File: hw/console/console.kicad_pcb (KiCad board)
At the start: 2 copper layers, 156 x 74 mm, 161 parts, among them J1 Batt, J301 USB-C 16P, J401 DM3AT-SF-PEJM5, J501 SPK 8R, J601 FFC-40 0.5mm, J901 UART, Q601 AO3400A, SW1 Движок, SW101 UP, SW102 DOWN, SW103 LEFT, SW104 RIGHT, SW105 SELECT, SW106 START, SW107 A, SW108 B, SW109 C, SW110 D, U1 F133-A, U2 SY8089AAAC, U3 SY8089AAAC, U4 SY8089AAAC, U401 W25Q32JVSSIQ, U5 TP4056, U501 PAM8301, Y1 24 МГц, Y2 32.768 кГц

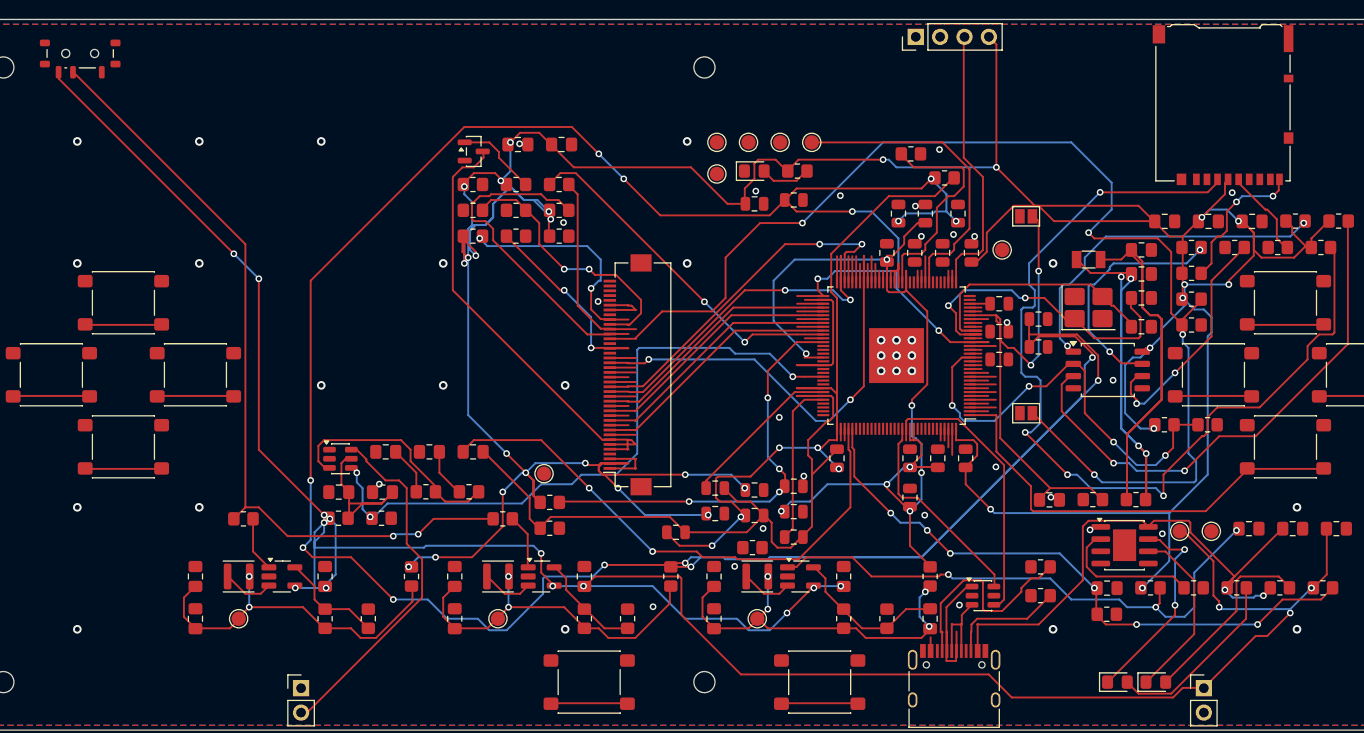
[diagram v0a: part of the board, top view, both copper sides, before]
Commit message: hw: плата на SPI разведена — 196 связей, 56 разрывов
Против параллельной версии: 203/67 при 270 нужных связях стало 196/56 при 252.
Меди 1198 отрезков, заклёпок 216 — их паять руками с двух сторон.

Нарушений DRC одно, проверенное: контур `J601` нарисован в библиотеке
прямоугольником, а на плате полигоном; все 41 площадка совпадает и по имени,
и по месту.

Co-Authored-By: Claude Opus 5 (1M context) <noreply@anthropic.com>
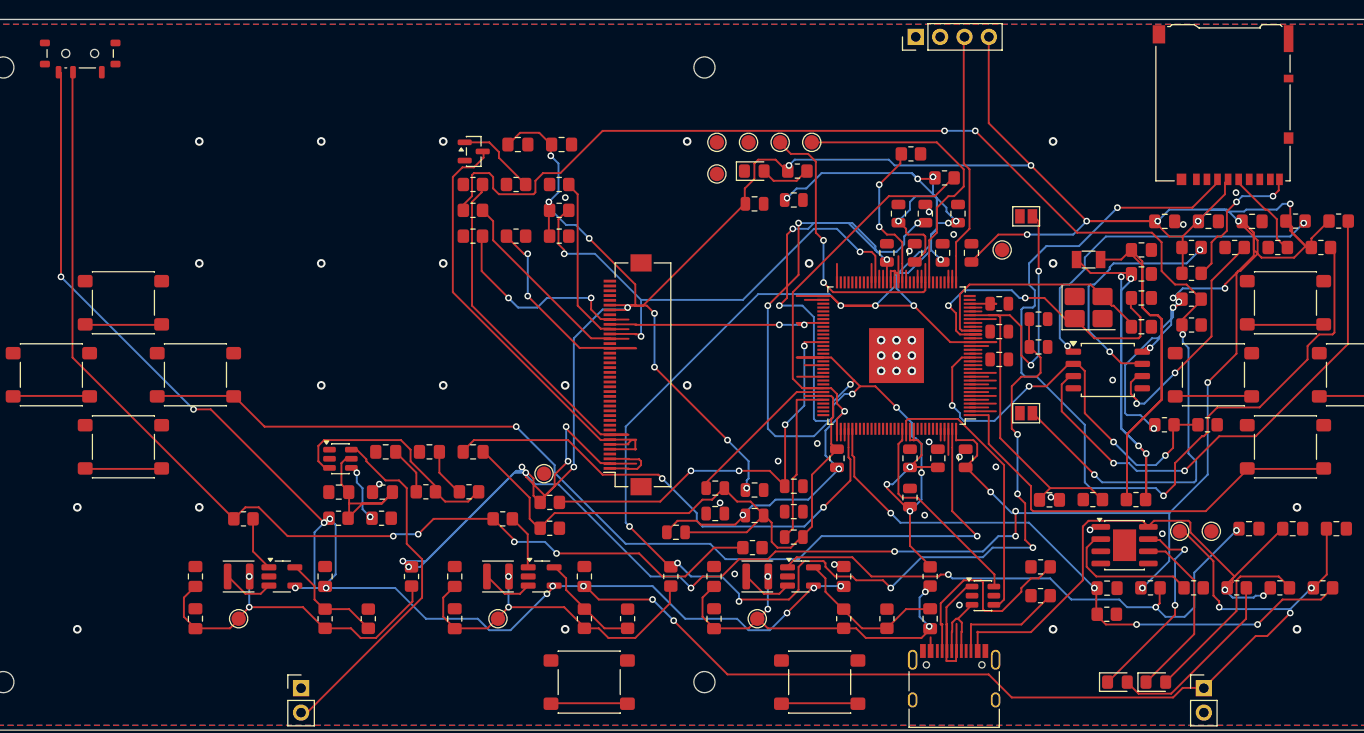
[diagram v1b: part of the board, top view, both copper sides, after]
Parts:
- removed R605: 33, Resistor_SMD:R_0805_2012Metric_Pad1.20x1.40mm_HandSolder
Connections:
- net LCD-WR renamed LCD-SCL
- J601 pad 10: LCD-RS -> LCD-DC
- J601 pad 13: SPI0-MOSI -> LCD-SDA
- J601 pad 17: LCD-DB0 -> GND
- J601 pad 18: LCD-DB1 -> GND
- J601 pad 19: LCD-DB2 -> GND
- J601 pad 20: LCD-DB3 -> GND
- J601 pad 21: LCD-DB4 -> GND
- J601 pad 22: LCD-DB5 -> GND
- J601 pad 23: LCD-DB6 -> GND
- J601 pad 24: LCD-DB7 -> GND
- J601 pad 25: LCD-DB8 -> GND
- J601 pad 26: LCD-DB9 -> GND
- J601 pad 27: LCD-DB11 -> GND
- J601 pad 28: LCD-DB10 -> GND
- J601 pad 29: LCD-DB12 -> GND
- J601 pad 30: LCD-DB13 -> GND
- J601 pad 31: LCD-DB14 -> GND
- J601 pad 32: LCD-DB15 -> GND
- R603 pad 1: LCD0-CLK -> SPI0-CLK
- R604 pad 1: LCD0-DE -> SPI0-MOSI
- R604 pad 2: LCD-RS -> LCD-SDA
- U1 pad 56: LCD-DB0 -> unconnected-(U1-PD1-Pad56)
- U1 pad 57: LCD-DB1 -> unconnected-(U1-PD2-Pad57)
- U1 pad 58: LCD-DB2 -> unconnected-(U1-PD3-Pad58)
- U1 pad 59: LCD-DB3 -> unconnected-(U1-PD4-Pad59)
- U1 pad 60: LCD-DB4 -> unconnected-(U1-PD5-Pad60)
- U1 pad 61: LCD-DB5 -> unconnected-(U1-PD6-Pad61)
- U1 pad 62: LCD-DB6 -> unconnected-(U1-PD7-Pad62)
- U1 pad 63: LCD-DB7 -> unconnected-(U1-PD8-Pad63)
- U1 pad 67: LCD-DB8 -> unconnected-(U1-PD10-Pad67)
- U1 pad 68: LCD-DB9 -> unconnected-(U1-PD11-Pad68)
- U1 pad 69: LCD-DB11 -> unconnected-(U1-PD13-Pad69)
- U1 pad 70: LCD-DB10 -> unconnected-(U1-PD12-Pad70)
- U1 pad 71: LCD-DB12 -> unconnected-(U1-PD14-Pad71)
- U1 pad 72: LCD-DB13 -> LCD-DC
- U1 pad 73: LCD-DB14 -> unconnected-(U1-PD16-Pad73)
- U1 pad 74: LCD-DB15 -> unconnected-(U1-PD17-Pad74)
- U1 pad 75: LCD0-CLK -> unconnected-(U1-PD18-Pad75)
- U1 pad 76: LCD0-DE -> unconnected-(U1-PD19-Pad76)
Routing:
- net +1V8: track 345.3 -> 234.2 mm, vias 16 -> 17
- net KEY-RIGHT: track 10.7 -> 106.1 mm, vias 0 -> 2
- net AMP-SD: track 68.3 -> 9.04 mm, vias 3 -> 2
- net +3V3: track 444.5 -> 492.2 mm, vias 29 -> 36
- net LCD-DB1: track 47.2 -> 0.00 mm, vias 2 -> 0
- net +0V9: track 104.9 -> 149.3 mm, vias 8 -> 13
- net LCD-DB6: track 37.6 -> 0.00 mm, vias 2 -> 0
- net LCD-DB7: track 37.5 -> 0.00 mm, vias 2 -> 0
- net LCD0-CLK: track 36.6 -> 0.00 mm, vias 2 -> 0
- net LCD-LEDA: track 2.75 -> 36.7 mm
- net /PWR_EN: track 82.3 -> 112.9 mm, vias 2 -> 4
- net TDO: track 2.72 -> 31.4 mm, vias 0 -> 2
- net LCD-RS: track 27.9 -> 0.00 mm, vias 2 -> 0
- net LCD-DB15: track 26.6 -> 0.00 mm
- net LCD-DB13: track 26.5 -> 0.00 mm
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
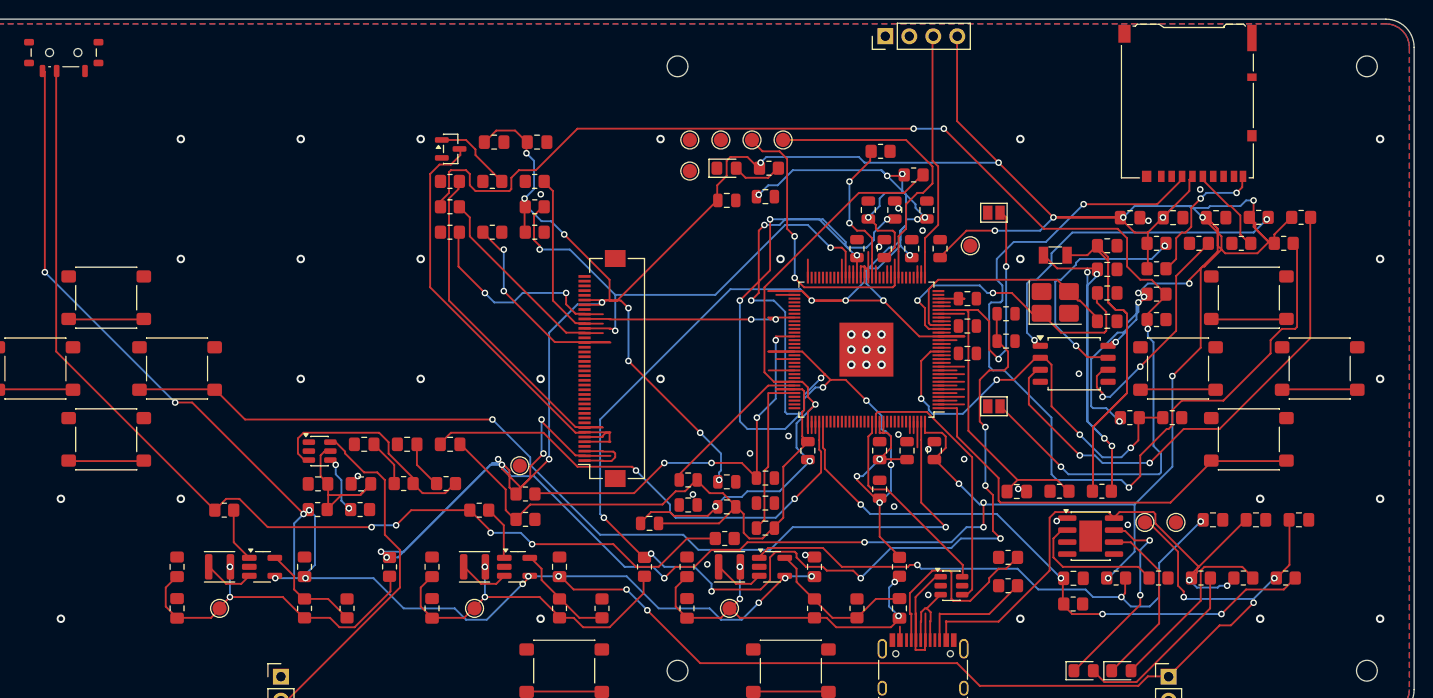
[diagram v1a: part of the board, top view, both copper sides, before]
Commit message: hw: обвязка флешки — к флешке, а не рядами в поле
Увидено заказчиком на снимке платы: `U401` стоит у выводов корпуса, а её девять
резисторов и конденсатор выложены ровным рядом в двух сантиметрах, и каждый
тянет провод обратно. По числам это выглядело просто «связь разведена».

Причина была записана в документе и мной же сегодня стёрта: `pcb03_blocks.py`
кладёт детали внутри зоны ПО РАЗМЕРУ и про связи не знает вовсе. Я заменил эту
запись своим выводом «размещение не узкое место» — вывод строился на шести
опытах, но ни один из них не двигал обвязку к её хозяину.

Теперь `pcb04_fine.py` ставит развязку, подтяжки и страпы относительно самой
`U401`: было 20…25 мм, стало 3.6…8.7.

Co-Authored-By: Claude Opus 5 (1M context) <noreply@anthropic.com>
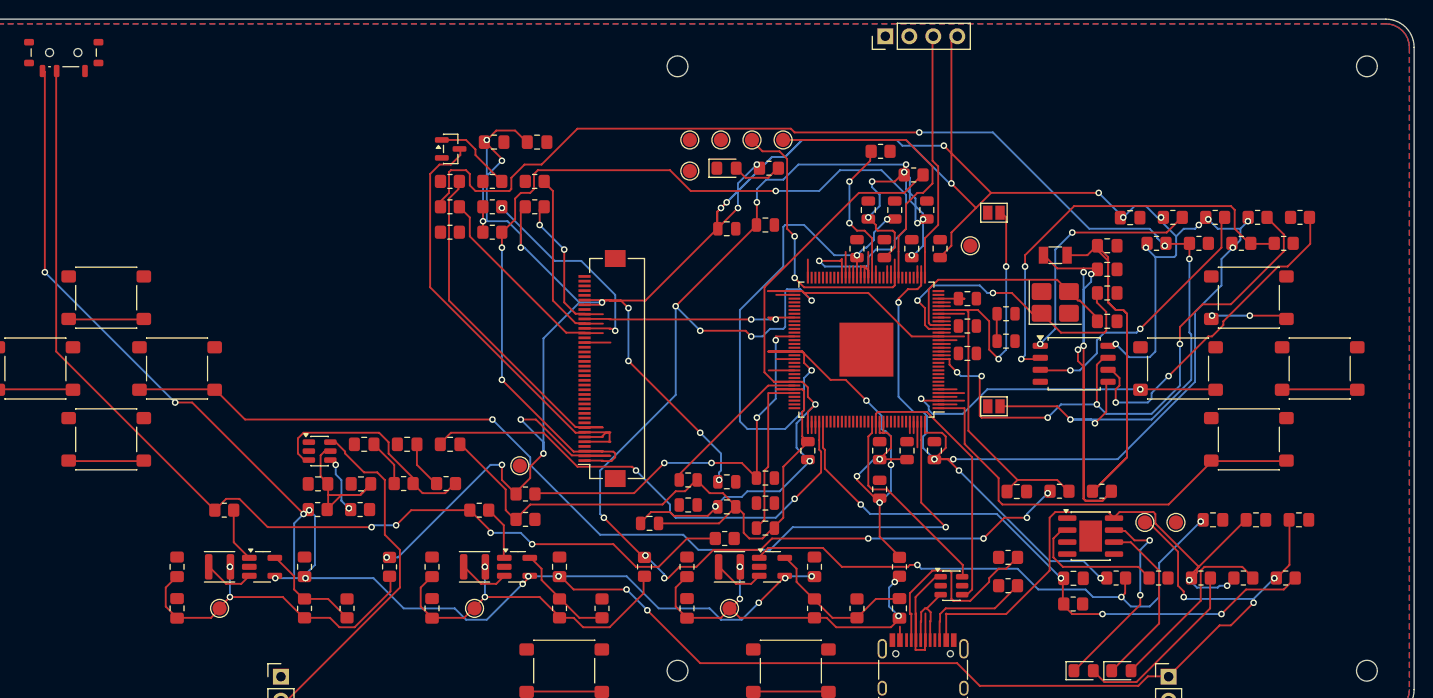
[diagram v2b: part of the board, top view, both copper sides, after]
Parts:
- removed C402: 0.1u, Capacitor_SMD:C_0805_2012Metric_Pad1.18x1.45mm_HandSolder
- removed C403: 10u, Capacitor_SMD:C_0805_2012Metric_Pad1.18x1.45mm_HandSolder
- removed J401: DM3AT-SF-PEJM5, Connector_Card:microSD_HC_Hirose_DM3AT-SF-PEJM5
- removed R405: 33, Resistor_SMD:R_0805_2012Metric_Pad1.20x1.40mm_HandSolder
- removed R406, R407: 10k, Resistor_SMD:R_0805_2012Metric_Pad1.20x1.40mm_HandSolder
- moved R411 21.9 mm to (192.2, 63.7)
- moved R410 21.9 mm to (187.7, 63.7)
- moved R403 11.1 mm to (189.4, 61.0)
- moved R404 11.1 mm to (193.9, 61.0)
- moved R607 9.37 mm to (112.9, 59.9)
- moved R409 9.23 mm to (183.2, 63.7)
- moved R401 9.10 mm to (180.4, 61.0)
- moved R402 9.10 mm to (184.9, 61.0)
- moved R408 5.38 mm to (178.7, 63.7)
- moved R608 4.49 mm to (103.9, 62.6)
- moved R606 4.49 mm to (108.4, 59.9)
- moved R609 4.49 mm to (108.4, 62.6)
- moved C803 3.00 mm to (133.2, 62.2)
- moved C812 3.00 mm to (137.3, 61.8)
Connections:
- U1 pad 10: SDC0-CMD -> unconnected-(U1-PF3-Pad10)
- U1 pad 11: SDC0-D3 -> unconnected-(U1-PF4-Pad11)
- U1 pad 12: SDC0-D2 -> unconnected-(U1-PF5-Pad12)
- U1 pad 13: SDC0-DET -> unconnected-(U1-PF6-Pad13)
- U1 pad 7: SDC0-D1 -> unconnected-(U1-PF0-Pad7)
- U1 pad 8: SDC0-D0 -> unconnected-(U1-PF1-Pad8)
- U1 pad 9: SDC0-CLK -> unconnected-(U1-PF2-Pad9)
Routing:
- net SDC0-CMD: track 99.5 -> 0.00 mm, vias 2 -> 0
- net LCD-IM: track 9.27 -> 107.3 mm, vias 0 -> 4
- net +3V3: track 492.2 -> 426.5 mm, vias 36 -> 33
- net SPI0-HOLD: track 26.4 -> 64.1 mm, vias 2 -> 5
- net +0V9: track 149.3 -> 111.8 mm, vias 13 -> 8
- net LCD-RD: track 53.8 -> 26.0 mm, vias 3 -> 2
- net KEY-B: track 9.93 -> 37.8 mm, vias 0 -> 2
- net SPI0-WP: track 56.2 -> 30.0 mm
- net +1V8: track 234.2 -> 211.6 mm, vias 17 -> 19
- net LCD-RST: track 25.5 -> 4.67 mm, vias 2 -> 0
- net SDC0-DET: track 16.4 -> 0.00 mm, vias 2 -> 0
- net SPI0-CS0: track 37.6 -> 26.9 mm
- net NOR-CLK: track 25.2 -> 35.2 mm
- net SD-CLK: track 9.39 -> 0.00 mm
- net X32KIN: track 57.2 -> 64.3 mm
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
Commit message: hw: дисплей на SPI1 — в блоке ноль переходных
Было 6 переходных, 16 пересечений по воздуху, 321.6 мм меди.
Стало 0, 0 и 201.6 мм, DRC чистый.

Разъём шлейфа слева от чипа, а SPI0 выходит на противоположную
сторону корпуса — такт и данные обходили чип кругом. SPI1 прибит к
PD11/PD12, то есть к нужной стороне, и вдобавок умеет DBI. Остальные
сигналы легли на соседние свободные выводы в порядке выводов разъёма,
поэтому дорожки идут параллельными полосами и не пересекаются.

RD и IM к чипу не идут вовсе: они были нужны только для переключения
между параллельным режимом и SPI, а параллельного режима больше нет.
Ушла самая длинная цепь блока.

Дорожки проложены руками, таблицей полос (pcb_hand.py): трассировщик
о полосах не знает и запечатывает соседа. Плата разбирается на блоки
(pcb_park.py), смотрится глазами и по пересечению лучей (pcb_view.py).

Co-Authored-By: Claude Opus 5 (1M context) <noreply@anthropic.com>
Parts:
- removed H1, H2, H3, H4, H5, H6: MountingHole_2.2mm_M2, MountingHole_2.2mm_M2
- moved C4 231.4 mm to (299.0, 40.0)
- moved C7 213.6 mm to (281.0, 46.0)
- moved R1 208.1 mm to (293.0, 64.0)
- moved R504 205.2 mm to (299.0, 76.0)
- moved R503 203.7 mm to (293.0, 76.0)
- moved R7 195.3 mm to (275.0, 82.0)
- moved C8 193.4 mm to (287.0, 46.0)
- moved L1 192.5 mm to (269.0, 64.0)
- moved R2 184.9 mm to (275.0, 70.0)
- moved R502 184.0 mm to (287.0, 76.0)
- moved R501 182.5 mm to (281.0, 76.0)
- moved C2 181.0 mm to (287.0, 40.0)
- moved R801 175.3 mm to (287.0, 82.0)
- moved R3 174.5 mm to (287.0, 70.0)
- moved R8 174.3 mm to (281.0, 82.0)
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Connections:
- R603 pad 1: SPI0-CLK -> SPI1-CLK
- R604 pad 1: SPI0-MOSI -> SPI1-MOSI
- U1 pad 52: LCD-BL -> unconnected-(U1-PD22-Pad52)
- U1 pad 53: LCD-CS -> unconnected-(U1-PD21-Pad53)
- U1 pad 54: LCD-RD -> unconnected-(U1-PD20-Pad54)
- U1 pad 55: LCD-IM -> unconnected-(U1-PD0-Pad55)
- U1 pad 64: LCD-RST -> LCD-CS
- U1 pad 67: unconnected-(U1-PD10-Pad67) -> LCD-DC
- U1 pad 68: unconnected-(U1-PD11-Pad68) -> SPI1-CLK
- U1 pad 70: unconnected-(U1-PD12-Pad70) -> SPI1-MOSI
- U1 pad 71: unconnected-(U1-PD14-Pad71) -> LCD-RST
- U1 pad 72: LCD-DC -> unconnected-(U1-PD15-Pad72)
- U1 pad 85: unconnected-(U1-PB3-Pad85) -> LCD-BL
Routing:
- net +3V3: track 426.5 -> 19.5 mm, vias 33 -> 0
- net VSYS: track 251.0 -> 0.00 mm, vias 17 -> 0
- net +1V8: track 211.6 -> 14.0 mm, vias 19 -> 0
- net SPI0-MOSI: track 138.9 -> 2.72 mm, vias 5 -> 0
- net /PWR_EN: track 112.9 -> 0.00 mm, vias 4 -> 0
- net KEY-RIGHT: track 106.1 -> 2.72 mm, vias 2 -> 0
- net +0V9: track 111.8 -> 10.4 mm, vias 8 -> 0
- net LCD-IM: track 107.3 -> 16.3 mm, vias 4 -> 0
- net AGND: track 74.0 -> 1.93 mm
- net AVCC: track 73.8 -> 4.65 mm, vias 3 -> 0
- net SPI0-HOLD: track 64.1 -> 1.93 mm, vias 5 -> 0
- net GPADC0: track 64.4 -> 2.72 mm, vias 4 -> 0
- net X32KIN: track 64.3 -> 2.72 mm, vias 4 -> 0
- net X32KOUT: track 63.3 -> 1.93 mm
- net EN_0V9: track 58.2 -> 0.00 mm, vias 3 -> 0
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
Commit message: hw: десять кнопок разведены, ноль переходных
Крестовина у левого края, кнопки действия у правого, между ними
семьдесят миллиметров. Четыре линии крестовины идут одной полосой
вдоль низа платы на y 91…93.4, SELECT и START поднимаются правее
корпуса, A обходит B между рядами её лапок.

Порядок выводов внутри обеих групп переставлен под геометрию: вывод
должен стоять там же по порядку, где подходит дорожка, иначе дорожки
пересекаются. DRC чистый, переходных нет.

Полоса держится вверху коридора нарочно: y 96…113 оставлено под USB и
звук, им тоже идти с нижнего края на чип.

Co-Authored-By: Claude Opus 5 (1M context) <noreply@anthropic.com>
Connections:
- U1 pad 1: KEY-C -> KEY-SELECT
- U1 pad 125: KEY-DOWN -> KEY-RIGHT
- U1 pad 126: KEY-LEFT -> KEY-DOWN
- U1 pad 127: KEY-RIGHT -> KEY-LEFT
- U1 pad 2: KEY-A -> KEY-START
- U1 pad 3: KEY-B -> KEY-C
- U1 pad 4: KEY-D -> KEY-B
- U1 pad 5: KEY-SELECT -> KEY-A
- U1 pad 6: KEY-START -> KEY-D
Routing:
- net KEY-LEFT: track 2.72 -> 130.1 mm
- net KEY-UP: track 1.92 -> 115.6 mm
- net KEY-DOWN: track 2.72 -> 104.6 mm
- net KEY-RIGHT: track 2.72 -> 103.2 mm
- net KEY-SELECT: track 1.93 -> 82.6 mm
- net KEY-START: track 2.72 -> 65.1 mm
- net KEY-A: track 2.72 -> 46.5 mm
- net KEY-D: track 2.72 -> 43.9 mm
- net KEY-C: track 1.93 -> 39.4 mm
- net KEY-B: track 1.93 -> 29.7 mm
